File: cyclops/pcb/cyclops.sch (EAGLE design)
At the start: 169 parts, among them Q4 IRF510, U1 MCP4921, U11 THS4281, U12 MAX4564, U13 ZXTD, U14 ZXTD, U15 OPA1664, U2 LT1931, U3 LT1764A, U4 BD60HC5WEFJ, U5 TPS72325, U6 LT1711, U7 TLV3701, U8 ADR03, U9 LT1880

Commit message: More routing and notes.
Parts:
- removed R5: 50, jonnew:R_1206
- added C40: 10uF, jonnew:C_1206
- C15: device cyclops:C_1206 -> jonnew:C_0603
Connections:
- removed net N$48: C13.1, C16.1, U5.GND
- removed net N$53: R5.1, VAUX_IN.1
- net +13.3V: now also C40.1; no longer C12.1, U4.EN, U4.VI
- net +15V: now also C12.1, U4.EN, U4.VI
- net +6V: now also C6.1, L3G$2.2, U2.VIN, U2.~SHDN, U4.VO
- net GND: now also C13.1, C16.1, C40.2, U4.GND, U5.GND
- net VAUX: now also VAUX_IN.1; no longer R5.2
- net VIN: no longer C6.1, L3G$2.2, U2.VIN, U2.~SHDN
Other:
- moved on the sheet: +6V, C12, C14, D2, L1, U4

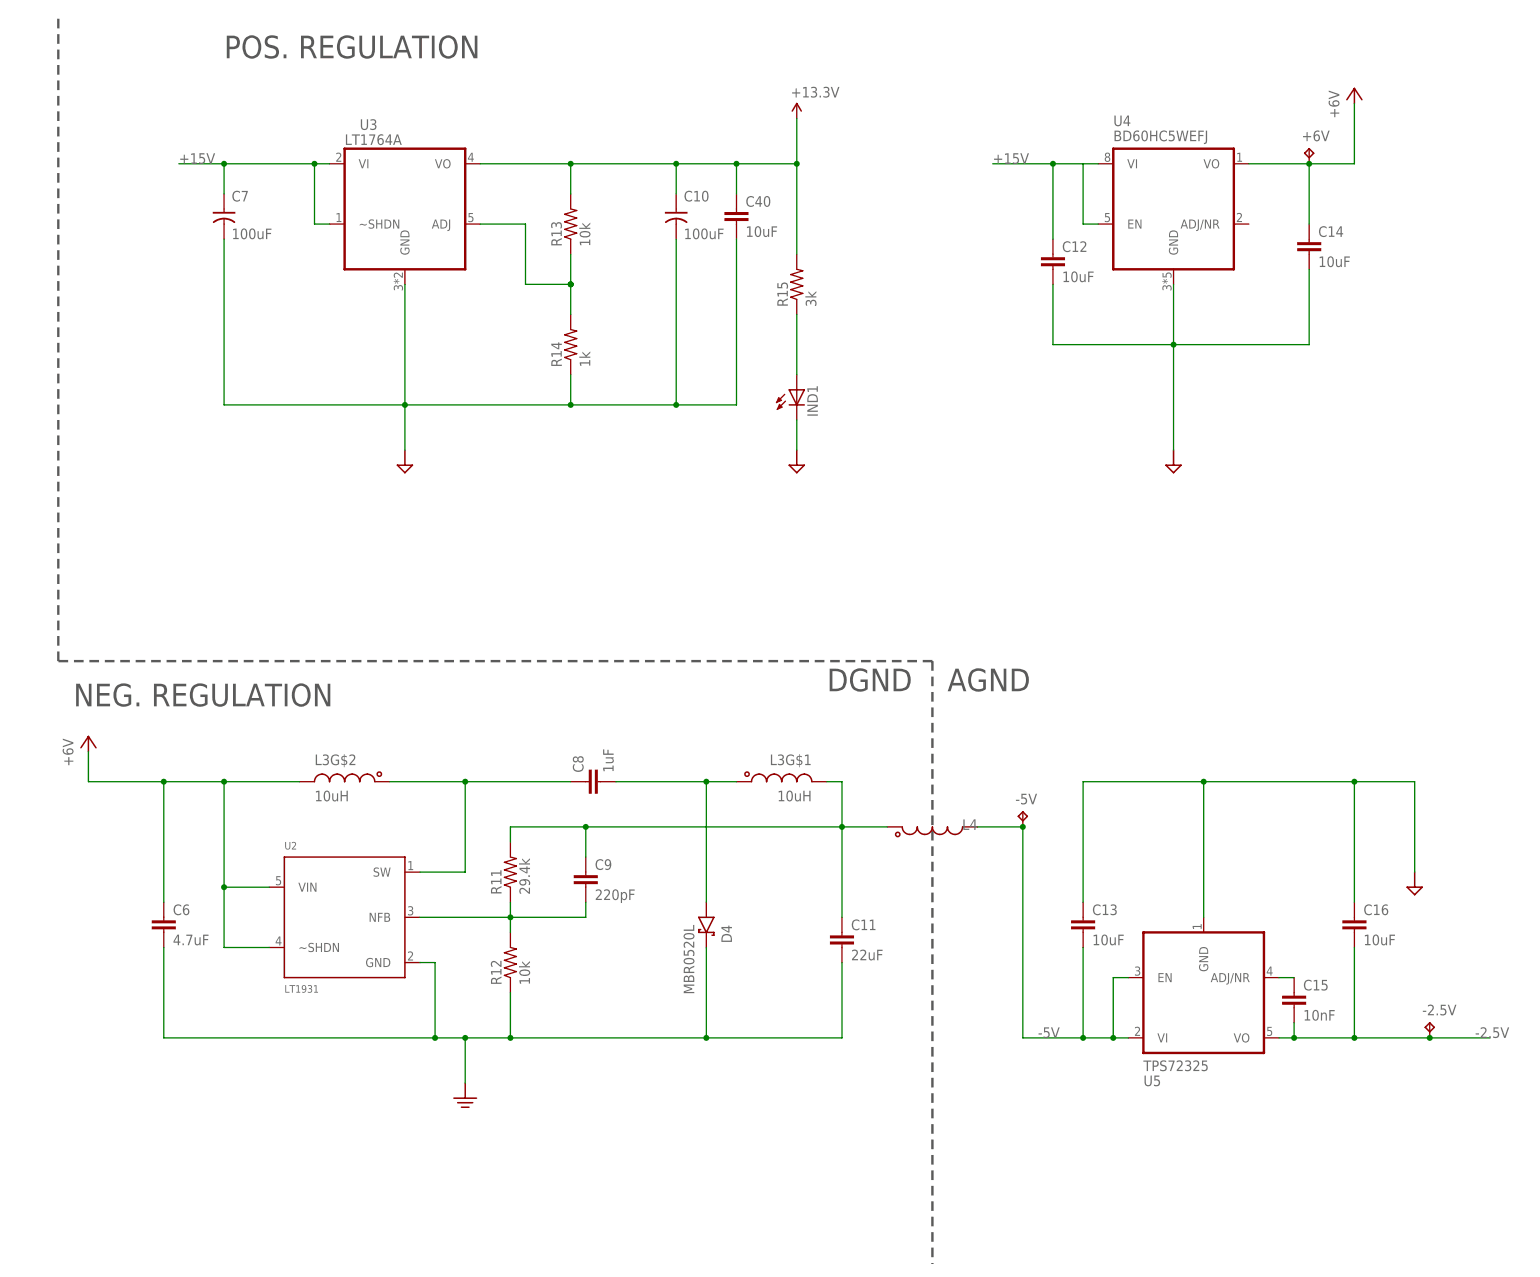
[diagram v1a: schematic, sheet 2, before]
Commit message: Started addining buck converter for digital rail.
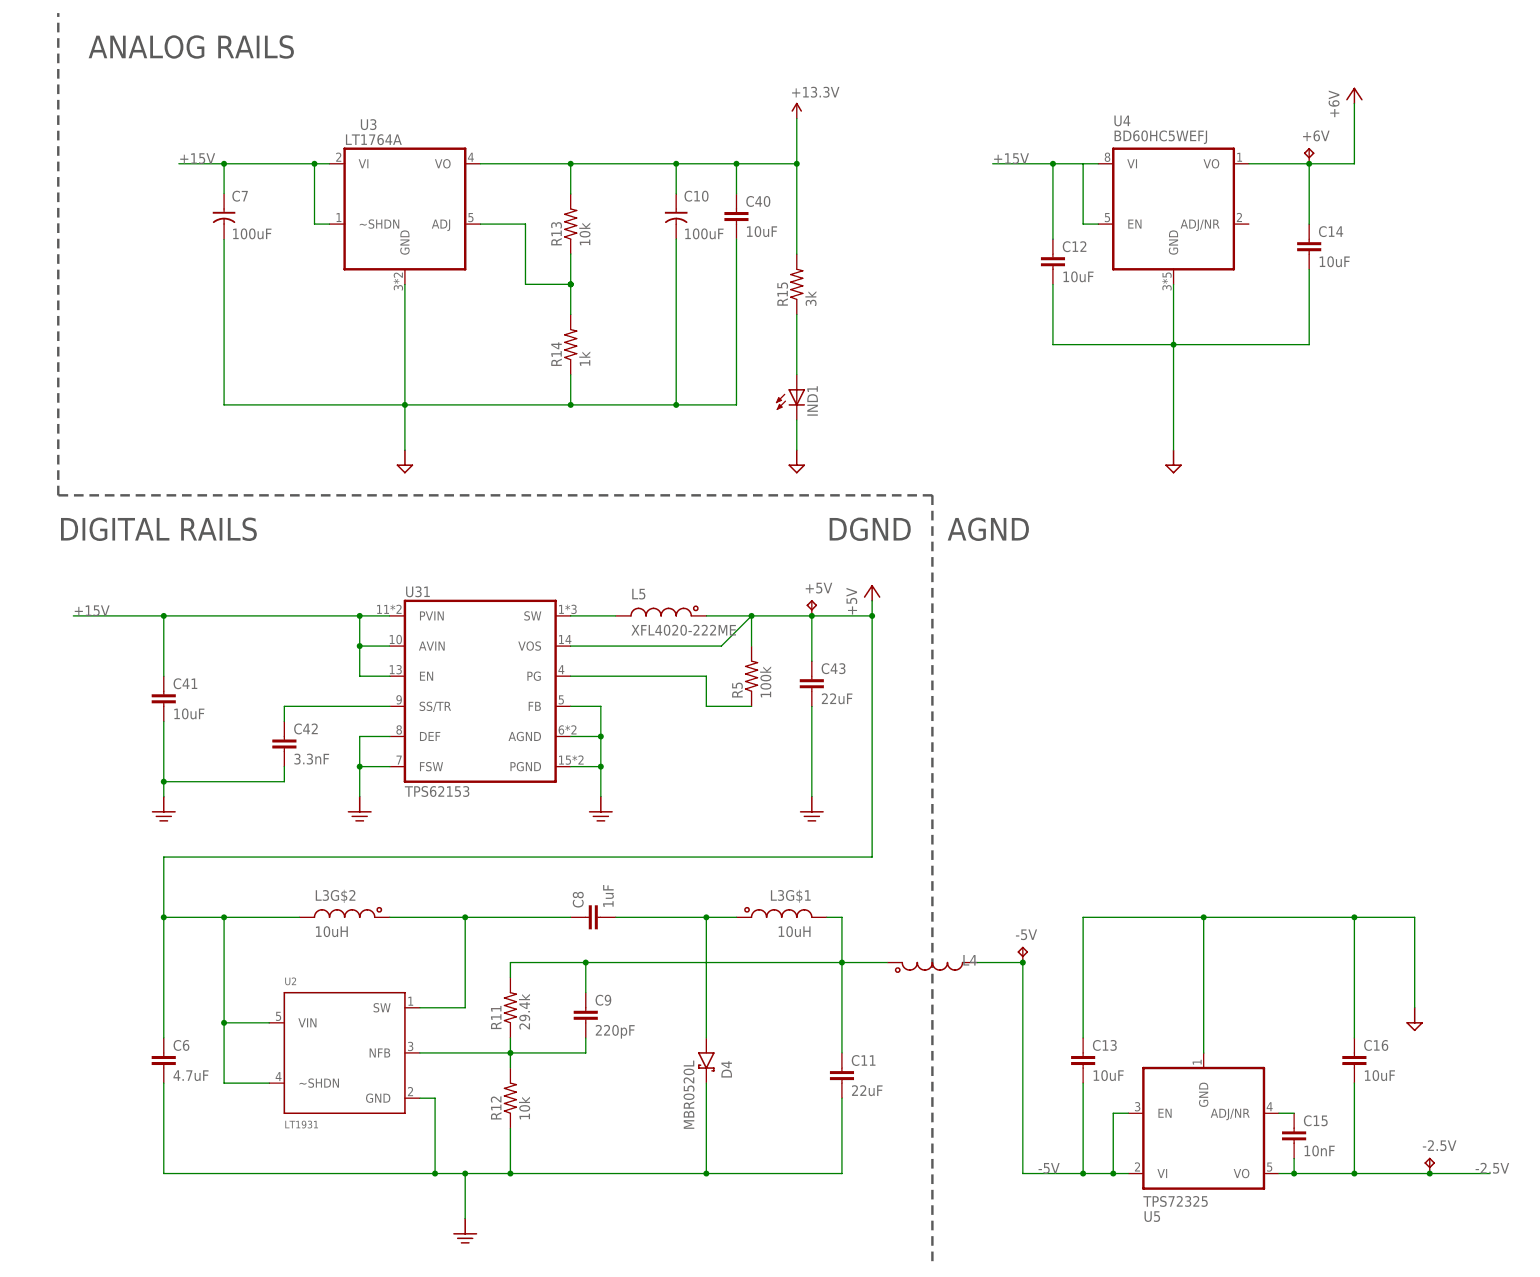
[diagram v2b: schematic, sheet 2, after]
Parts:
- removed L1: MPZ1608, cyclops:L_0603
- added +5V: TPTP16R, cyclops:TPTP16R
- added C41: 10uF, jonnew:C_1206
- added C42: 3.3nF, jonnew:C_0603
- added C43: 22uF, jonnew:C_2220
- added L5: XFL4020-222ME, jonnew:L_4020
- added R5: 100k, cyclops:R_0603
- added U31: TPS62153, jonnew:TPS6125X_VQFN16
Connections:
- net VIN renamed TEENSY_VIN
- removed net N$43: D2.A, L1.1
- new net +5V: +5V.TP, C43.1, C6.1, D2.A, L3G$2.2, L5.1, R5.2, U2.VIN, U2.~SHDN, U31.VOS
- new net N$48: U31.DEF, U31.FSW
- new net N$53: C41.2, C42.2
- new net N$56: C42.1, U31.SS/TR
- new net N$59: C43.2
- new net PG: R5.1, U31.PG
- new net SW: L5.2, U31.SW
- net +15V: now also C41.1, U31.AVIN, U31.EN, U31.PVIN
- net +6V: no longer C6.1, L1.2, L3G$2.2, U2.VIN, U2.~SHDN
- net GND: now also U31.AGND, U31.FB, U31.PGND
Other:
- note added: "ANALOG RAILS"
- note added: "DIGITAL RAILS"
- note removed: "NEG. REGULATION"
- note removed: "POS. REGULATION"
- moved on the sheet: -2.5V, -5V, C11, C13, C15, C16, C6, C8, C9, D2, D4, L3G$1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

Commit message: Buck converter and 6V LDO added.
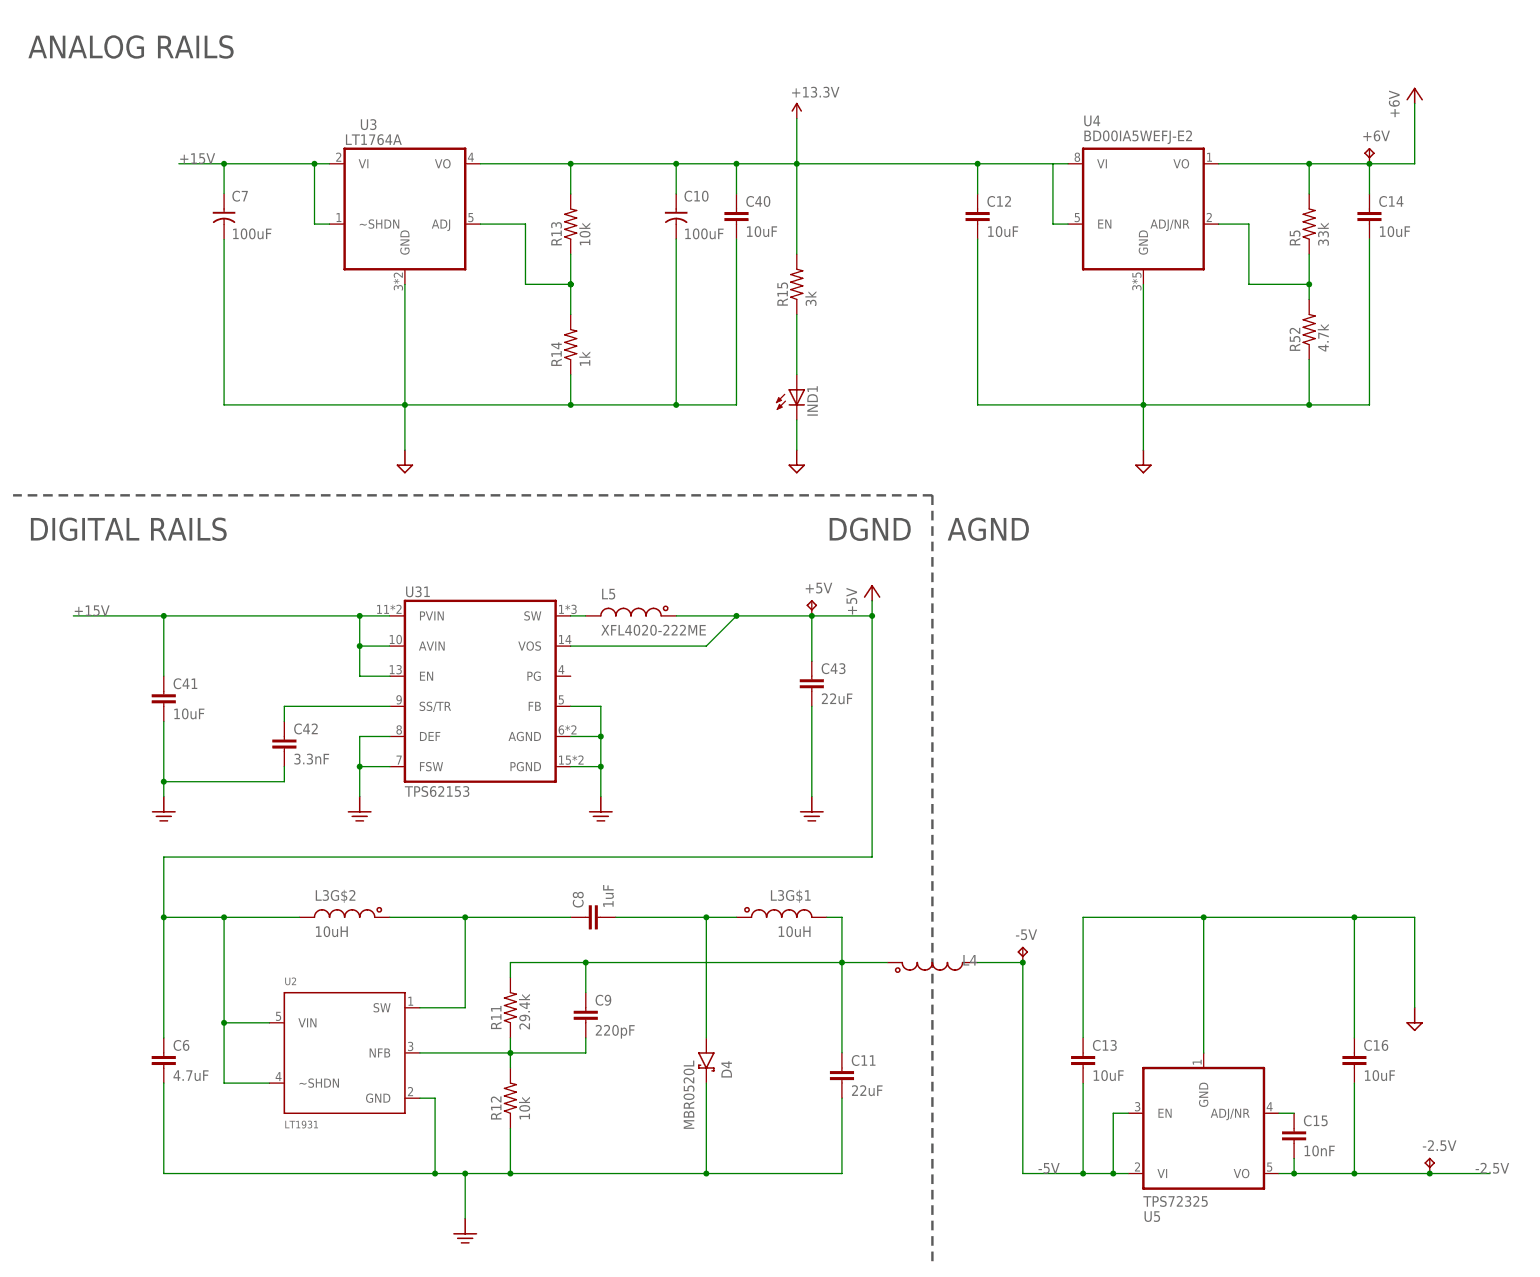
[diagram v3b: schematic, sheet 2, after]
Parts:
- added D5, D6: STPS0560Z, jonnew:S-DIODESOD-123
- added R52: 4.7k, cyclops:R_0603
- C43: device jonnew:C_2220 -> jonnew:C_0805
- J_ADDR1, J_ADDR2, J_ADDR3, J_ADDR4, J_CS1, J_CS2, J_CS3, J_CS4, J_LDAC1, J_LDAC2, J_LDAC3, J_LDAC4, J_OC1, J_OC2, J_OC3, J_OC4, J_T1, J_T2, J_T3, J_T4: device cyclops:R_0603 -> jonnew:R_0402
- R10: device cyclops:R_0603 -> jonnew:R_0805
- R5: value 100k -> 33k
- U4: value BD60HC5WEFJ -> BD00IA5WEFJ-E2; device jonnew:LDO_ADJUST_BDXXHC5WEFJ -> jonnew:LDO_ADJUST_BDXXFC0
- renumbered REF2.1 to REF2V5, REF5.1 to REF5V0
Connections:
- removed net N$59: C43.2
- removed net PG: R5.1, U31.PG
- removed net V+: C24.1, C25.1, U9G$2.V+
- new net N$43: R5.1, R52.2, U4.ADJ/NR
- net +13.3V: now also C12.1, U4.EN, U4.VI
- net +15V: no longer C12.1, U4.EN, U4.VI
- net +5V: no longer R5.2
- net +6V: now also C24.1, C25.1, R5.2, U9G$2.V+
- net GND: now also C41.2, C42.2, C43.2, R52.1, U31.DEF, U31.FSW
- net N$48: now also D6.A; no longer U31.DEF, U31.FSW
- net N$53: now also D5.C; no longer C41.2, C42.2
- net VAUX: now also D5.A, D6.C
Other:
- moved on the sheet: +6V, C12, C14, L2, L5, R4, R5, U4, VAUX_IN, VAUX_OUT
